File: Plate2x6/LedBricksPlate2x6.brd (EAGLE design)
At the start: 44 x 12 mm, 8 parts

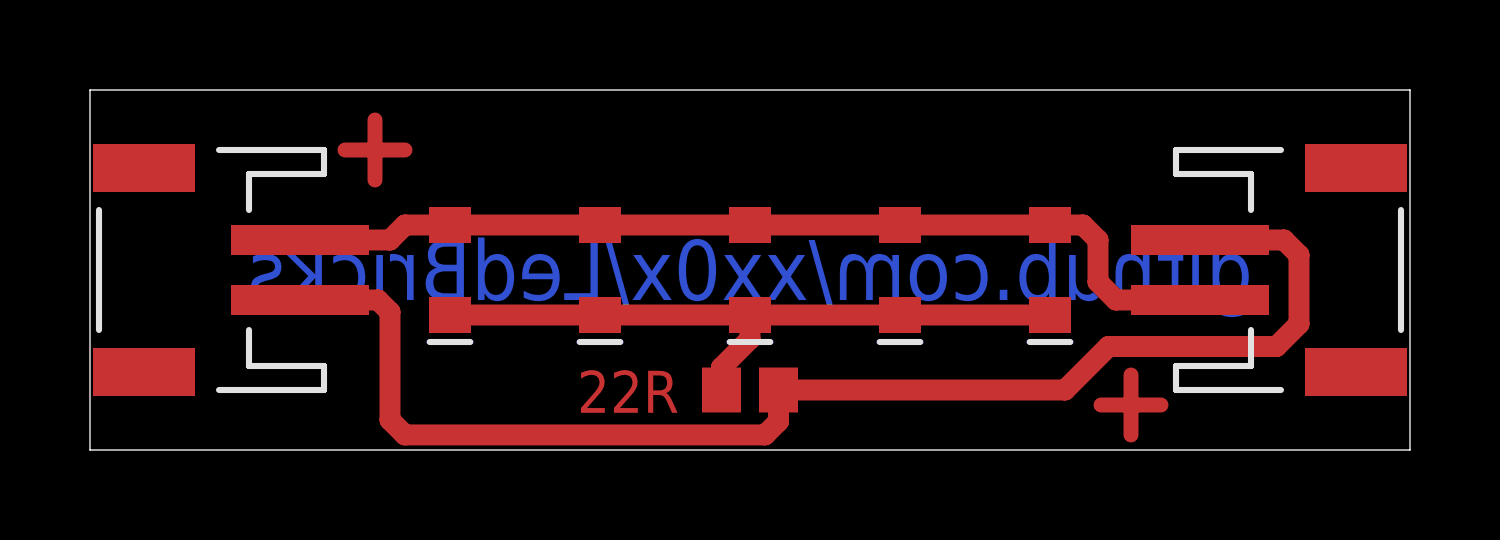
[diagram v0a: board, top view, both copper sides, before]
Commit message: change connector to jst sh
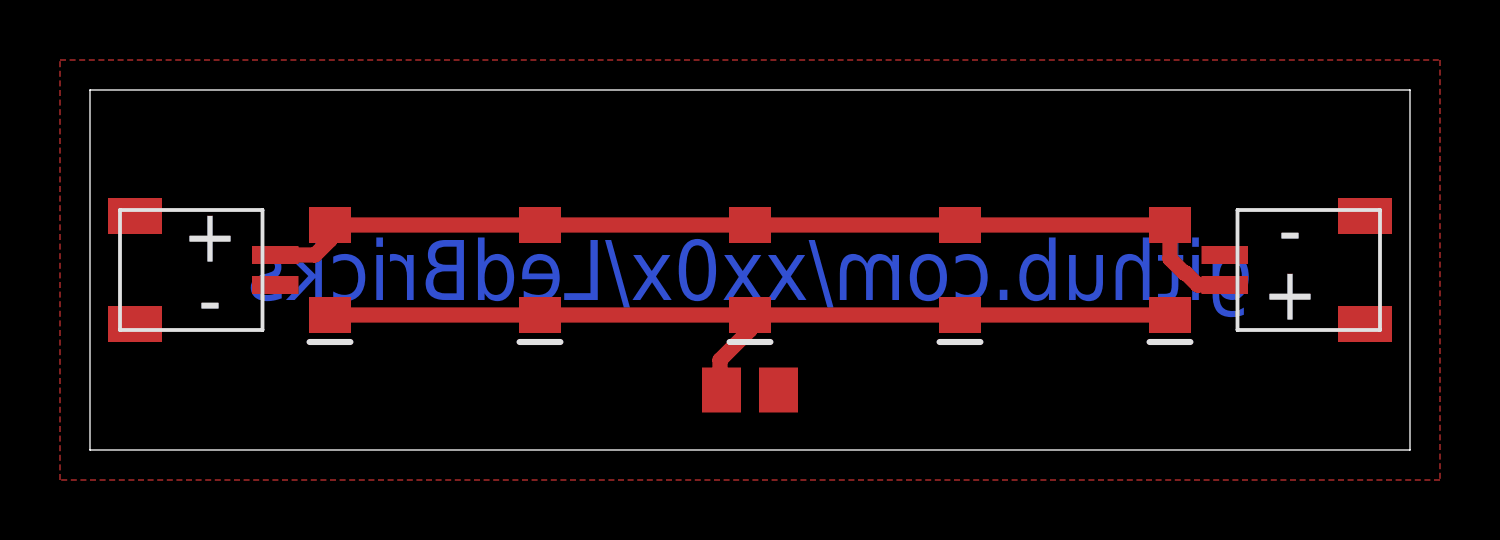
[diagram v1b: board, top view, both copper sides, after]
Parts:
- J1, J2: value (none) -> SM02B-SRSS-TB; device SparkFun-Connectors:JST-2-SMD -> con-JST-SH:SM02B-SRSS-TB
- moved J1 39.2 mm to (1.50, 6.00)
- moved J2 39.2 mm to (42.5, 6.00)
- moved D1 4.00 mm to (8.00, 6.00)
- moved D5 4.00 mm to (36.0, 6.00)
- moved D2 2.00 mm to (15.0, 6.00)
- moved D4 2.00 mm to (29.0, 6.00)
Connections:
- net +5V: now also J1.1, J2.1; no longer J1.2, J2.2
- net GND: now also J1.2, J2.2; no longer J1.1, J2.1
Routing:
- net GND: track 45.2 -> 0.00 mm
- net N$2: track 22.9 -> 30.9 mm
- net N$5: track 2.00 -> 0.00 mm
- net N$4: track 2.00 -> 0.00 mm
- net N$3: track 2.00 -> 0.00 mm
- net N$1: track 2.00 -> 0.00 mm
- net +5V: track 32.1 -> 33.8 mm
- added copper zone on layer 1, net GND
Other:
- board text added: "+ -"
- board text added: "- +"

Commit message: gerbers, pnp file
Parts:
- D1, D2, D3, D4, D5: value (none) -> XL-3216WWC
- moved R1 3.62 mm to (18.7, 3.50), turned to 90 degrees
- moved D1 1.00 mm to (9.00, 6.00)
- moved D5 1.00 mm to (35.0, 6.00)
- moved D2 0.50 mm to (15.5, 6.00)
- moved D4 0.50 mm to (28.5, 6.00)
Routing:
- net N$2: track 30.9 -> 26.0 mm
- added copper zone on layer 16, net GND
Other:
- board text added: "+"
- board text added: "-"
- board text removed: "+ -"
- board text removed: "- +"
